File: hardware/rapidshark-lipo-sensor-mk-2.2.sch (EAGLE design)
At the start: 13 parts, among them IC1 Tiny84, Q1 2N7000, Q2 2N7000, Q3 2N7000

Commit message: lipo voltage testing boards
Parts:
- removed Q1, Q2, Q3: 2N7000, a_parts:MOSFET-NCHANNEL2N7000
- added C1, C2, C3: 100n, A_butts:CAPACITOR-CERAMIC025-024X044
- added R5, R6: 10k, A_butts:RESISTORPTH-AXIAL-5.08MM
- BATT: value M04JST_XH_VERT -> M04PTH; device a_parts:M04JST_XH_VERT -> a_parts:M04PTH
- FRAME1: VERSION v2.0 -> v2.2
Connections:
- removed net EN1: IC1.(PCINT8/XTAL1/CLKI)PB0, Q1.G
- removed net EN2: IC1.(PCINT9/XTAL2)PB1, Q2.G
- removed net EN3: IC1.(PCINT10/INT0/OC0A/CKOUT)PB2, Q3.G
- removed net N$3: Q3.D, R4.1
- net BATT-: now also C1.2, R1.1; no longer R1.2
- net CELL1+: now also C2.2, R3.1
- net CELL2+: now also C3.2, R4.2, R5.1; no longer R3.2
- net CELL3+: now also R6.2; no longer R4.2
- net VDIV1: now also C1.1, R1.2, R2.1; no longer Q1.S, R1.1
- net VDIV2: now also C2.1, R3.2, R4.1; no longer Q1.D, Q2.S, R2.1
- net VDIV3: now also C3.1, R5.2, R6.1; no longer Q2.D, Q3.S, R3.1
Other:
- moved on the sheet: R1, R2, R3, R4

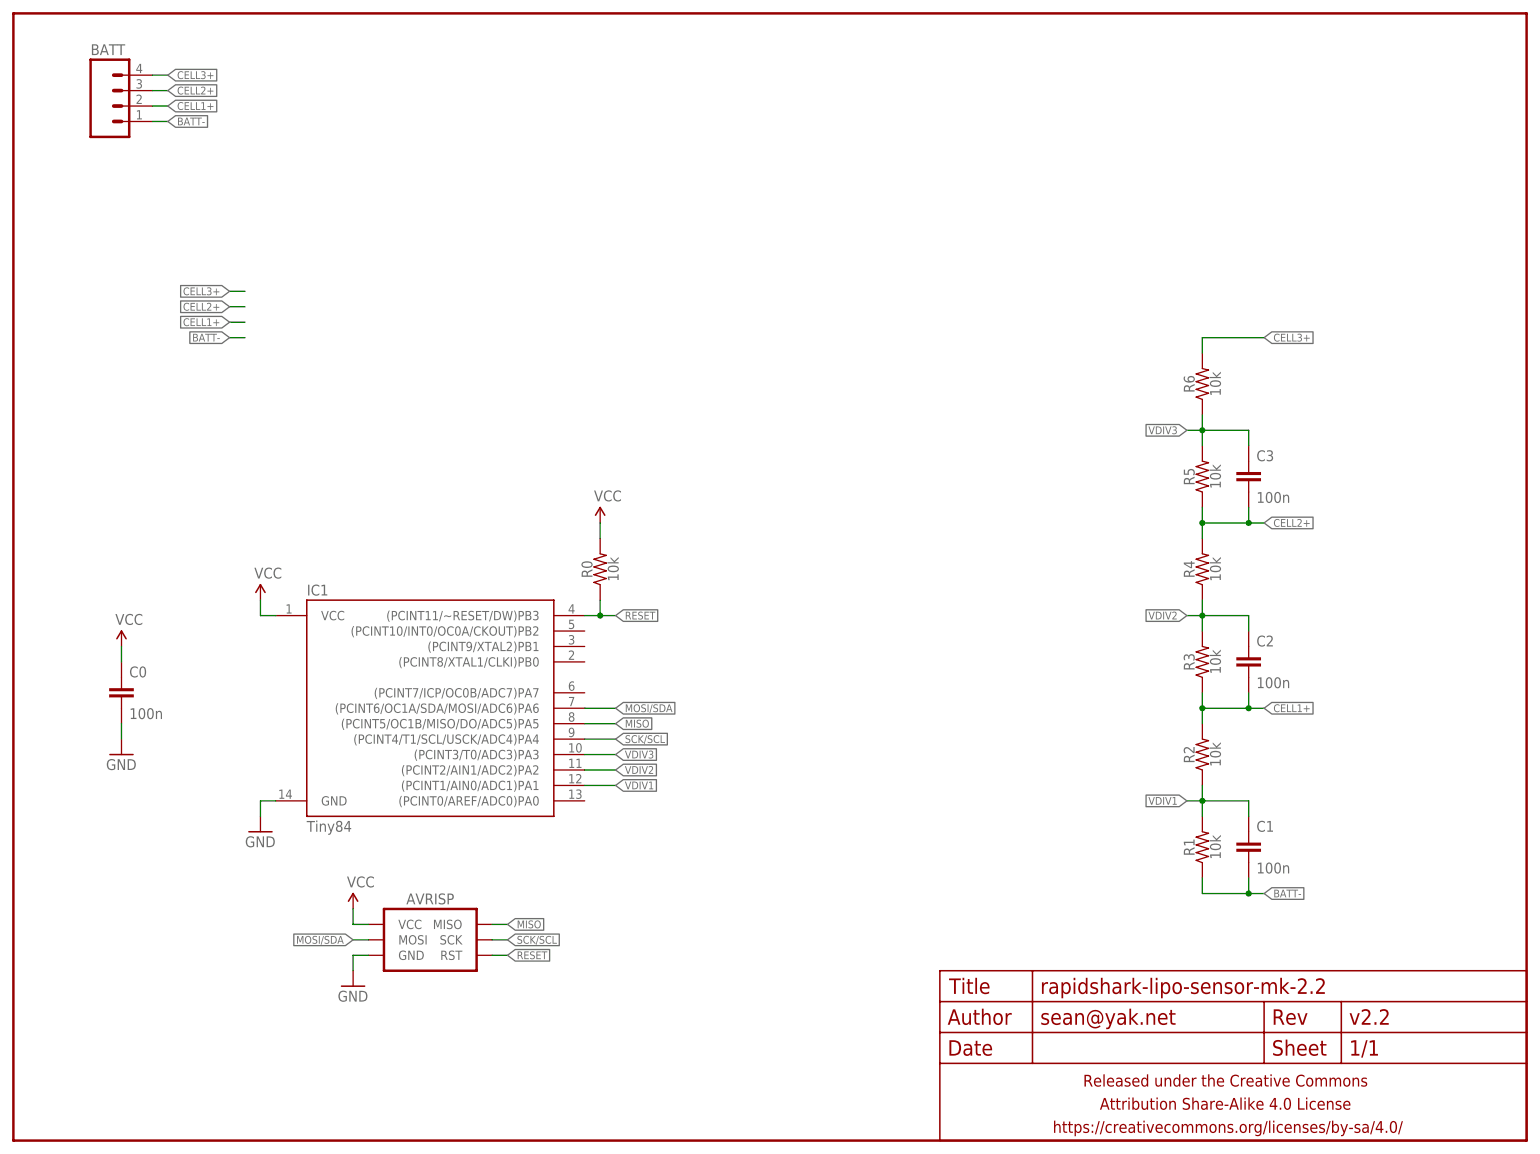
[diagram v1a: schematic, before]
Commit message: unfinished hardware design for a battery level tester which reports over SPI/I2c
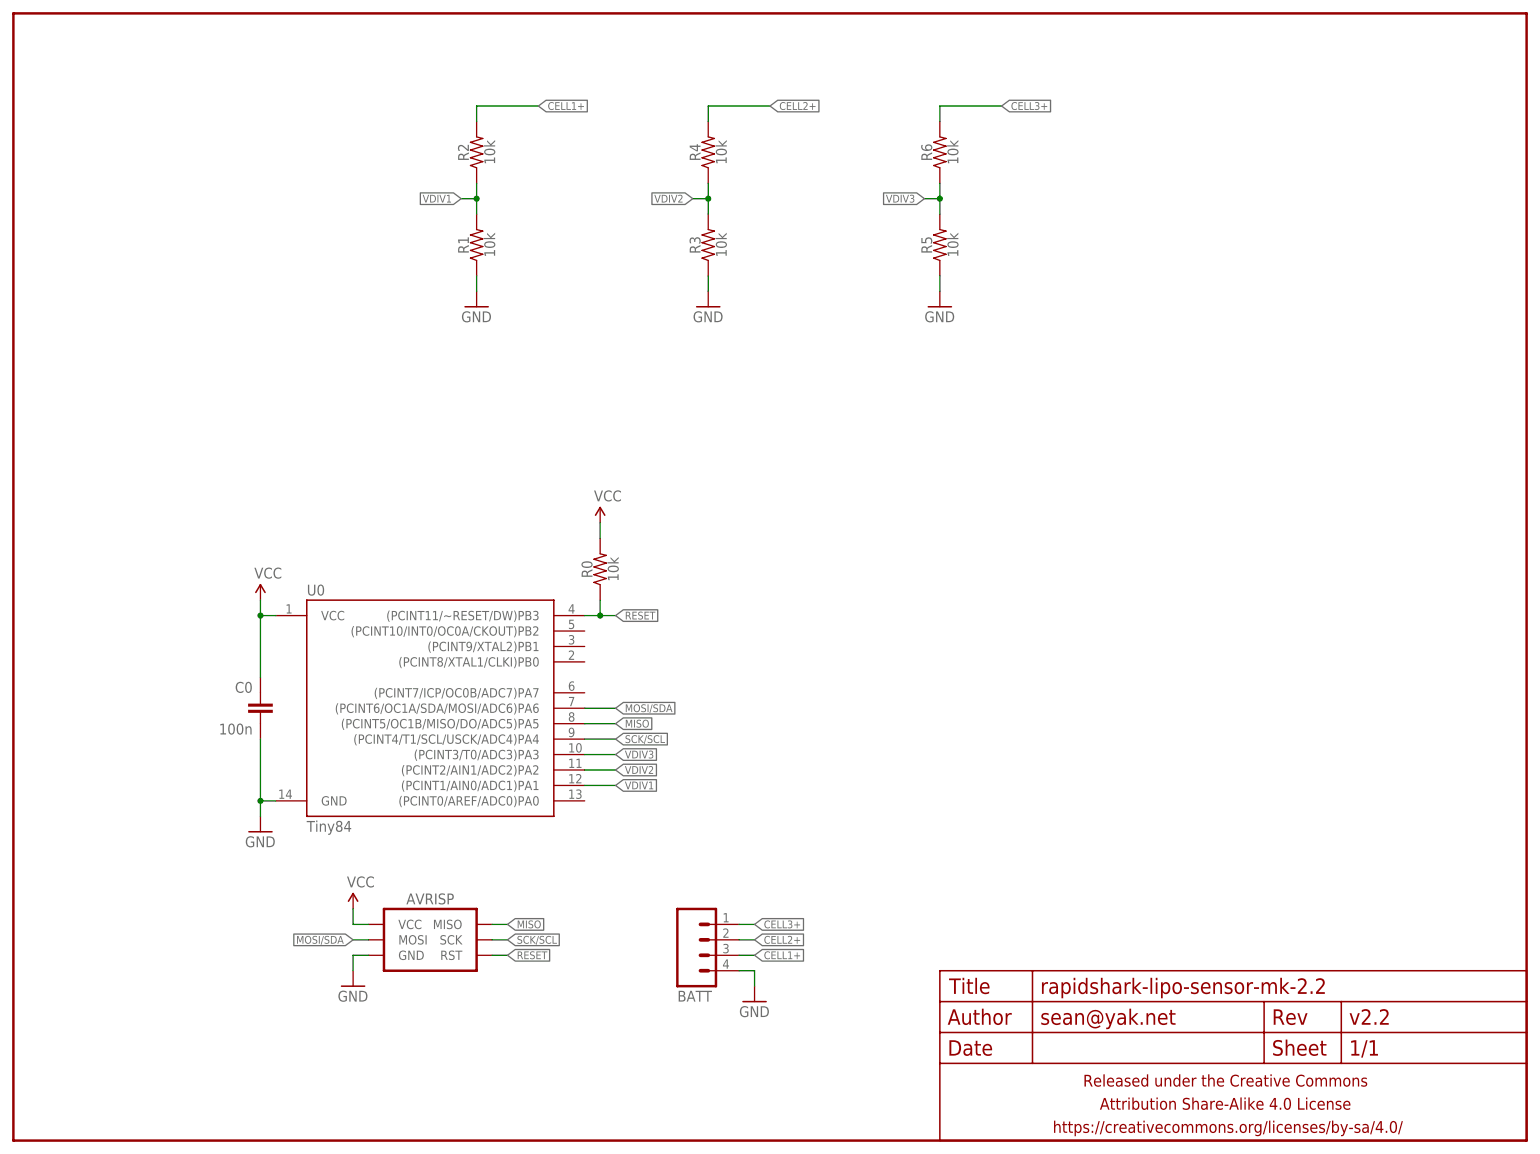
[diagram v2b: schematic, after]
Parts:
- removed C1, C2, C3: 100n, A_butts:CAPACITOR-CERAMIC025-024X044
- BATT: value M04PTH -> M04JST_XH_VERT; device a_parts:M04PTH -> a_parts:M04JST_XH_VERT
- renumbered IC1 to U0
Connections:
- removed net BATT-: BATT.1, C1.2, R1.1
- net CELL1+: now also BATT.3; no longer BATT.2, C2.2, R3.1
- net CELL2+: now also BATT.2; no longer BATT.3, C3.2, R5.1
- net CELL3+: now also BATT.1; no longer BATT.4
- net GND: now also BATT.4, R1.1, R3.1, R5.1
- net VDIV1: no longer C1.1
- net VDIV2: no longer C2.1
- net VDIV3: no longer C3.1
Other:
- moved on the sheet: BATT, C0, R1, R2, R3, R4, R5, R6
